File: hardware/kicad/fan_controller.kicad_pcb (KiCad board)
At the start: 2 copper layers, 75 x 60 mm, 75 parts, among them J1 12V IN, J10 AIN2, J11 AIN3, J12 AIN4, J13 AIN5, J14 AIN6, J2 BluePill A, J3 BluePill B, J5 FAN1, J6 FAN2, J7 FAN3, J8 FAN4, J9 AIN1, Q1 BSS138, Q2 BSS138, Q3 BSS138, Q4 BSS138

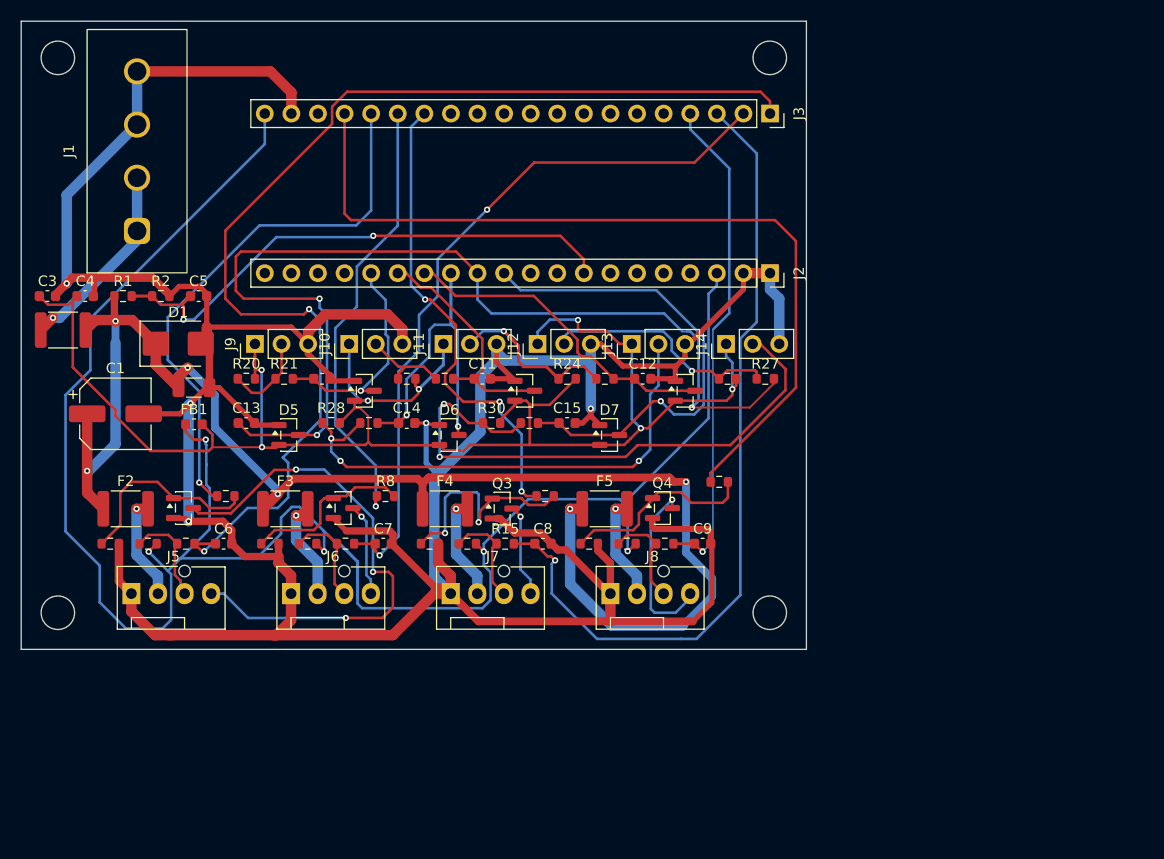
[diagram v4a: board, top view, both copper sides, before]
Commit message: DC mode support
Signed-off-by: Roman Skakun <rm.skakun@gmail.com>
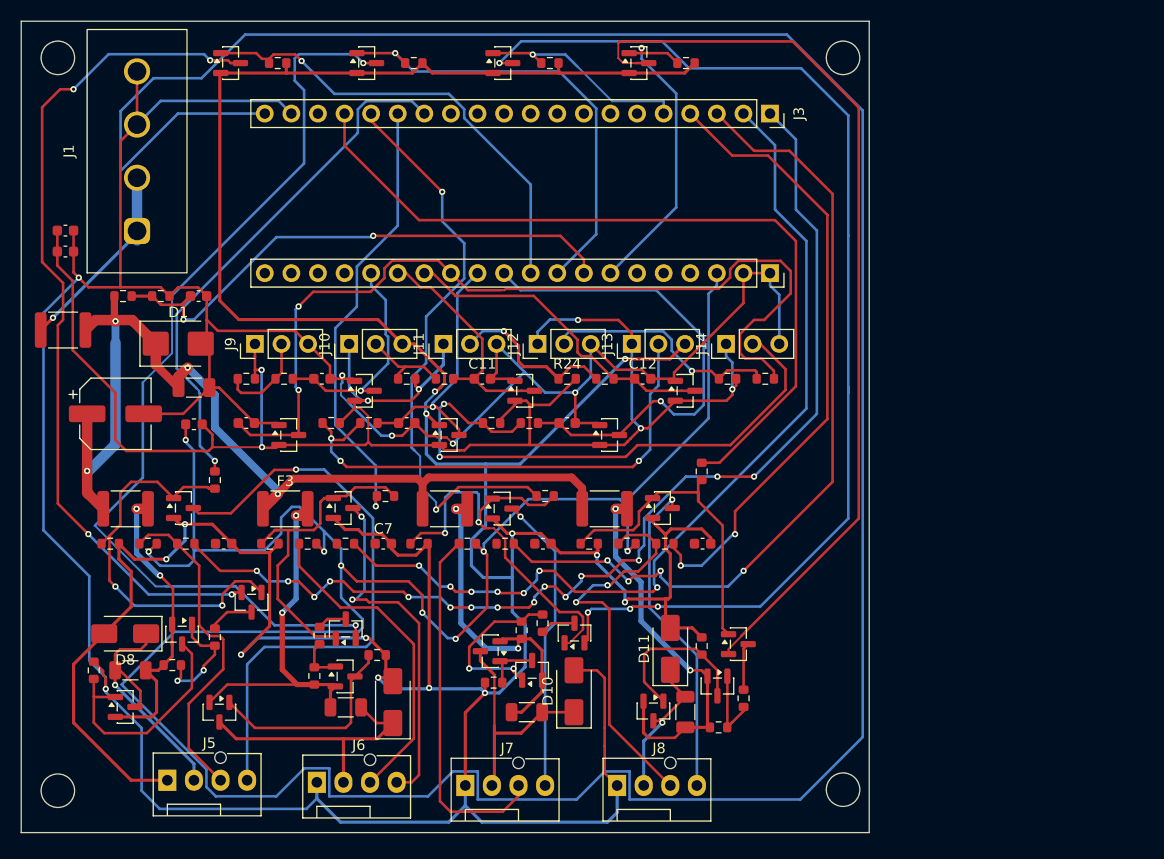
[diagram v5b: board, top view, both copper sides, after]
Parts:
- added D10: SS34, Diode_SMD:D_SMA, F.Cu at (52.8, 64.0)
- added D11: SS34, Diode_SMD:D_SMA, F.Cu at (62.0, 60.0)
- added D8: SS34, Diode_SMD:D_SMA, F.Cu at (9.93, 58.5)
- added D9: SS34, Diode_SMD:D_SMA, F.Cu at (35.5, 65.0)
- added JP1: 0, Resistor_SMD:R_1206_3216Metric, F.Cu at (10.4, 62.0)
- added JP2: 0, Resistor_SMD:R_1206_3216Metric, F.Cu at (31.0, 65.5)
- added JP3: 0, Resistor_SMD:R_1206_3216Metric, F.Cu at (48.3, 66.0)
- added JP4: 0, Resistor_SMD:R_1206_3216Metric, F.Cu at (63.4, 66.0)
- added Q10: BSS138, Package_TO_SOT_SMD:SOT-23, F.Cu at (31.0, 58.0)
- added Q11: AO3401A, Package_TO_SOT_SMD:SOT-23, F.Cu at (44.8, 60.2)
- added Q12: MMBT3906, Package_TO_SOT_SMD:SOT-23, F.Cu at (48.8, 62.0)
- added Q13: BSS138, Package_TO_SOT_SMD:SOT-23, F.Cu at (52.9, 58.4)
- added Q14: AO3401A, Package_TO_SOT_SMD:SOT-23, F.Cu at (60.4, 65.9)
- added Q15: MMBT3906, Package_TO_SOT_SMD:SOT-23, F.Cu at (66.5, 63.5)
- added Q16: BSS138, Package_TO_SOT_SMD:SOT-23, F.Cu at (68.5, 59.5)
- added Q17: BSS138, Package_TO_SOT_SMD:SOT-23, F.Cu at (20.0, 4.00)
- added Q18: BSS138, Package_TO_SOT_SMD:SOT-23, F.Cu at (33.0, 4.00)
- added Q19: BSS138, Package_TO_SOT_SMD:SOT-23, F.Cu at (46.0, 4.00)
- added Q20: BSS138, Package_TO_SOT_SMD:SOT-23, F.Cu at (59.0, 4.00)
- added Q5: AO3401A, Package_TO_SOT_SMD:SOT-23, F.Cu at (9.93, 65.5)
- added Q6: MMBT3906, Package_TO_SOT_SMD:SOT-23, F.Cu at (15.4, 58.5)
- added Q7: BSS138, Package_TO_SOT_SMD:SOT-23, F.Cu at (22.0, 55.5)
- added Q8: AO3401A, Package_TO_SOT_SMD:SOT-23, F.Cu at (18.9, 66.0)
- added Q9: MMBT3906, Package_TO_SOT_SMD:SOT-23, F.Cu at (30.9, 62.6)
- added R32: 2.2k, Resistor_SMD:R_0603_1608Metric, F.Cu at (6.93, 62.0)
- added R33: 10k, Resistor_SMD:R_0603_1608Metric, F.Cu at (14.4, 61.5)
- added R34: 4.7k, Resistor_SMD:R_0603_1608Metric, F.Cu at (18.5, 58.8)
- added R35: 2.2k, Resistor_SMD:R_0603_1608Metric, F.Cu at (34.0, 60.5)
- added R36: 10k, Resistor_SMD:R_0603_1608Metric, F.Cu at (28.0, 62.5)
- added R37: 4.7k, Resistor_SMD:R_0603_1608Metric, F.Cu at (28.5, 58.7)
- added R38: 2.2k, Resistor_SMD:R_0603_1608Metric, F.Cu at (45.1, 63.2)
- added R39: 10k, Resistor_SMD:R_0603_1608Metric, F.Cu at (47.8, 58.2)
- added R40: 4.7k, Resistor_SMD:R_0603_1608Metric, F.Cu at (49.8, 57.5)
- added R41: 2.2k, Resistor_SMD:R_0603_1608Metric, F.Cu at (65.0, 59.7)
- added R42: 10k, Resistor_SMD:R_0603_1608Metric, F.Cu at (66.6, 67.5)
- added R43: 4.7k, Resistor_SMD:R_0603_1608Metric, F.Cu at (69.0, 64.7)
- added R44: 10k, Resistor_SMD:R_0603_1608Metric, F.Cu at (24.5, 4.00)
- added R45: 10k, Resistor_SMD:R_0603_1608Metric, F.Cu at (37.5, 4.00)
- added R46: 10k, Resistor_SMD:R_0603_1608Metric, F.Cu at (50.5, 4.00)
- added R47: 10k, Resistor_SMD:R_0603_1608Metric, F.Cu at (63.5, 4.00)
- moved J7 18.4 mm to (42.4, 73.0)
- moved J8 18.3 mm to (56.9, 73.0)
- moved J6 18.2 mm to (28.2, 72.7)
- moved J5 18.2 mm to (14.0, 72.5)
- moved C3 6.49 mm to (4.22, 20.0)
- moved C4 4.66 mm to (4.22, 22.0)
- moved R16 1.95 mm to (65.0, 43.0), turned to -90 degrees
- moved R4 1.85 mm to (18.5, 43.8), turned to -90 degrees
- moved R13 1.01 mm to (38.0, 49.9)
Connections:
- net FAN1_TACH_IN renamed Net-(J5-Pad3)
- net FAN2_PWM renamed Net-(J3-Pad15)
- net FAN4_PWM renamed Net-(J3-Pad17)
- net FAN4_TACH_IN renamed Net-(J8-Pad3)
- F2 pad 2: FAN1_12V -> +12V_F1
- F3 pad 2: FAN2_12V -> Net-(F3-Pad2)
- F4 pad 2: FAN3_12V -> +12V_F3
- F5 pad 2: FAN4_12V -> +12V_F4
- J2 pad 10: (no net) -> FAN1_DCEN
- J2 pad 12: AIN4 -> AIN5
- J2 pad 13: AIN5 -> AIN4
- J2 pad 17: (no net) -> unconnected-(J2-PC15-Pad17)
- J2 pad 18: (no net) -> unconnected-(J2-PC14-Pad18)
- J2 pad 19: (no net) -> unconnected-(J2-PC13-Pad19)
- J2 pad 20: (no net) -> unconnected-(J2-VBAT-Pad20)
- J2 pad 5: (no net) -> /FAN4_SW
- J2 pad 6: (no net) -> /FAN3_SW
- J2 pad 7: (no net) -> FAN4_DCEN
- J2 pad 9: (no net) -> FAN2_DCEN
- J3 pad 1: FAN1_TACH -> Net-(J3-Pad1)
- J3 pad 10: (no net) -> /FAN1_SW
- J3 pad 11: (no net) -> /FAN2_SW
- J3 pad 12: (no net) -> unconnected-(J3-PB4-Pad12)
- J3 pad 13: (no net) -> unconnected-(J3-PB5-Pad13)
- J3 pad 14: FAN3_PWM -> Net-(J3-Pad14)
- J3 pad 16: FAN1_PWM -> Net-(J3-Pad16)
- J3 pad 2: FAN2_TACH -> Net-(J3-Pad2)
- J3 pad 3: FAN3_TACH -> Net-(J3-Pad3)
- J3 pad 4: FAN4_TACH -> Net-(J3-Pad4)
- J3 pad 5: (no net) -> FAN3_DCEN
- J3 pad 6: (no net) -> unconnected-(J3-PA9-Pad6)
- J3 pad 7: (no net) -> unconnected-(J3-PA10-Pad7)
- J6 pad 3: FAN2_TACH_IN -> Net-(J6-Pad3)
- J7 pad 3: FAN3_TACH_IN -> Net-(J7-Pad3)
- R10 pad 1: FAN2_TACH_IN -> Net-(J6-Pad3)
- R11 pad 2: FAN2_TACH -> Net-(J3-Pad2)
- R12 pad 1: FAN3_PWM -> Net-(J3-Pad16)
- R14 pad 1: FAN3_TACH_IN -> Net-(J7-Pad3)
- R15 pad 2: FAN3_TACH -> Net-(J3-Pad3)
- R19 pad 2: FAN4_TACH -> Net-(J3-Pad4)
- R4 pad 1: FAN1_PWM -> Net-(J3-Pad14)
- R7 pad 2: FAN1_TACH -> Net-(J3-Pad1)
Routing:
- net GND: track 364.3 -> 647.1 mm, vias 5 -> 19
- net +3V3: track 186.7 -> 396.7 mm, vias 5 -> 8
- net Net-(Q13-Pad2): track 0.00 -> 109.2 mm, vias 0 -> 4
- net FAN1_TACH: track 108.9 -> 0.00 mm, vias 2 -> 0
- net Net-(J3-Pad1): track 0.00 -> 105.0 mm, vias 0 -> 15
- net Net-(Q10-Pad2): track 0.00 -> 91.7 mm, vias 0 -> 2
- net Net-(Q16-Pad2): track 0.00 -> 87.7 mm
- net Net-(J3-Pad2): track 0.00 -> 87.1 mm, vias 0 -> 7
- net Net-(Q17-Pad3): track 0.00 -> 81.5 mm, vias 0 -> 4
- net Net-(J3-Pad3): track 0.00 -> 79.3 mm, vias 0 -> 4
- net FAN3_TACH: track 77.8 -> 0.00 mm, vias 1 -> 0
- net FAN2_TACH: track 68.9 -> 0.00 mm, vias 2 -> 0
- net Net-(J3-Pad4): track 0.00 -> 60.1 mm, vias 0 -> 2
- net Net-(J3-Pad16): track 0.00 -> 55.4 mm, vias 0 -> 2
- net FAN1_PWM: track 52.2 -> 0.00 mm, vias 1 -> 0
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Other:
- board size 75 x 60 mm -> 81 x 77.5 mm

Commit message: hw: fix schematic connectivity errors and sync PCB to new nets
Convert local labels to global labels so net names stop getting a
sheet-path prefix (/+12V vs +12V) on PCB sync. Add missing junction
markers at four T-tapped gate-drive/tach points that touch a crossing
wire's body but weren't bonded to it, and missing GND symbols on the
channel-1 gate-bias resistor, channel-3 flyback diode, and the AIN
clamp/filter network. Resolve a duplicate #PWR101 annotation. Sync the
PCB from the schematic now that nets match cleanly (ERC 57->17
violations, 41->13 errors).

Signed-off-by: Roman Skakun <rm.skakun@gmail.com>
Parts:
- added Q17: BSS138, Package_TO_SOT_SMD:SOT-23, F.Cu at (101.0, 30.2)
- added Q18: BSS138, Package_TO_SOT_SMD:SOT-23, F.Cu at (101.0, 34.7)
- added Q19: BSS138, Package_TO_SOT_SMD:SOT-23, F.Cu at (101.0, 39.1)
- added Q20: BSS138, Package_TO_SOT_SMD:SOT-23, F.Cu at (101.0, 43.6)
- added R44: 10k, Resistor_SMD:R_0603_1608Metric, F.Cu at (105.4, 29.3)
- added R45: 10k, Resistor_SMD:R_0603_1608Metric, F.Cu at (105.4, 31.8)
- added R46: 10k, Resistor_SMD:R_0603_1608Metric, F.Cu at (105.4, 34.3)
- added R47: 10k, Resistor_SMD:R_0603_1608Metric, F.Cu at (105.4, 36.8)
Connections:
- net Net-(F3-Pad2) renamed +12V_F2
- net Net-(J3-Pad14) renamed FAN1_PWM
- net Net-(J3-Pad15) renamed FAN2_PWM
- net Net-(J3-Pad16) renamed FAN3_PWM
- net Net-(J3-Pad17) renamed FAN4_PWM
- net Net-(J5-Pad3) renamed FAN1_TACH_IN
- net Net-(J8-Pad3) renamed FAN4_TACH_IN
- C1 pad 2: GND -> unconnected-(C1---Pad2)
- C2 pad 2: GND -> unconnected-(C2-Pad2)
- C3 pad 2: GND -> unconnected-(C3-Pad2)
- C4 pad 2: GND -> unconnected-(C4-Pad2)
- C5 pad 2: GND -> unconnected-(C5-Pad2)
- D1 pad 2: GND -> unconnected-(D1-A-Pad2)
- J1 pad 3: GND -> unconnected-(J1-Pad3)
- J1 pad 4: GND -> unconnected-(J1-Pad4)
- J2 pad 1: GND -> unconnected-(J2-GND-Pad1)
- J2 pad 2: GND -> unconnected-(J2-GND-Pad2)
- J2 pad 5: /FAN4_SW -> unconnected-(J2-PB11-Pad5)
- J2 pad 6: /FAN3_SW -> unconnected-(J2-PB10-Pad6)
- J3 pad 1: Net-(J3-Pad1) -> FAN1_TACH
- J3 pad 10: /FAN1_SW -> unconnected-(J3-PA15-Pad10)
- J3 pad 11: /FAN2_SW -> unconnected-(J3-PB3-Pad11)
- J3 pad 19: GND -> unconnected-(J3-GND-Pad19)
- J3 pad 2: Net-(J3-Pad2) -> FAN2_TACH
- J3 pad 3: Net-(J3-Pad3) -> FAN3_TACH
- J3 pad 4: Net-(J3-Pad4) -> FAN4_TACH
- J6 pad 3: Net-(J6-Pad3) -> FAN2_TACH_IN
- J7 pad 3: Net-(J7-Pad3) -> FAN3_TACH_IN
- Q10 pad 2: Net-(Q10-Pad2) -> Net-(Q10-S)
- Q13 pad 2: Net-(Q13-Pad2) -> Net-(Q13-S)
- Q16 pad 2: Net-(Q16-Pad2) -> Net-(Q16-S)
- Q7 pad 2: Net-(Q17-Pad3) -> Net-(Q17-D)
- R10 pad 1: Net-(J6-Pad3) -> FAN2_TACH_IN
- R11 pad 2: Net-(J3-Pad2) -> FAN2_TACH
- R14 pad 1: Net-(J7-Pad3) -> FAN3_TACH_IN
- R15 pad 2: Net-(J3-Pad3) -> FAN3_TACH
- R19 pad 2: Net-(J3-Pad4) -> FAN4_TACH
- R2 pad 2: GND -> unconnected-(R2-Pad2)
- R7 pad 2: Net-(J3-Pad1) -> FAN1_TACH
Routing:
- net Net-(J3-Pad1): track 105.0 -> 0.00 mm, vias 15 -> 0
- net FAN1_TACH: track 0.00 -> 105.0 mm, vias 0 -> 15
- net Net-(J3-Pad2): track 87.1 -> 0.00 mm, vias 7 -> 0
- net FAN2_TACH: track 0.00 -> 87.1 mm, vias 0 -> 7
- net Net-(J3-Pad3): track 79.3 -> 0.00 mm, vias 4 -> 0
- net FAN3_TACH: track 0.00 -> 79.3 mm, vias 0 -> 4
- net Net-(J3-Pad4): track 60.1 -> 0.00 mm, vias 2 -> 0
- net FAN4_TACH: track 0.00 -> 60.1 mm, vias 0 -> 2
- net Net-(J7-Pad3): track 34.9 -> 0.00 mm
- net FAN3_TACH_IN: track 0.00 -> 34.9 mm
- net Net-(J6-Pad3): track 31.1 -> 0.00 mm
- net FAN2_TACH_IN: track 0.00 -> 31.1 mm

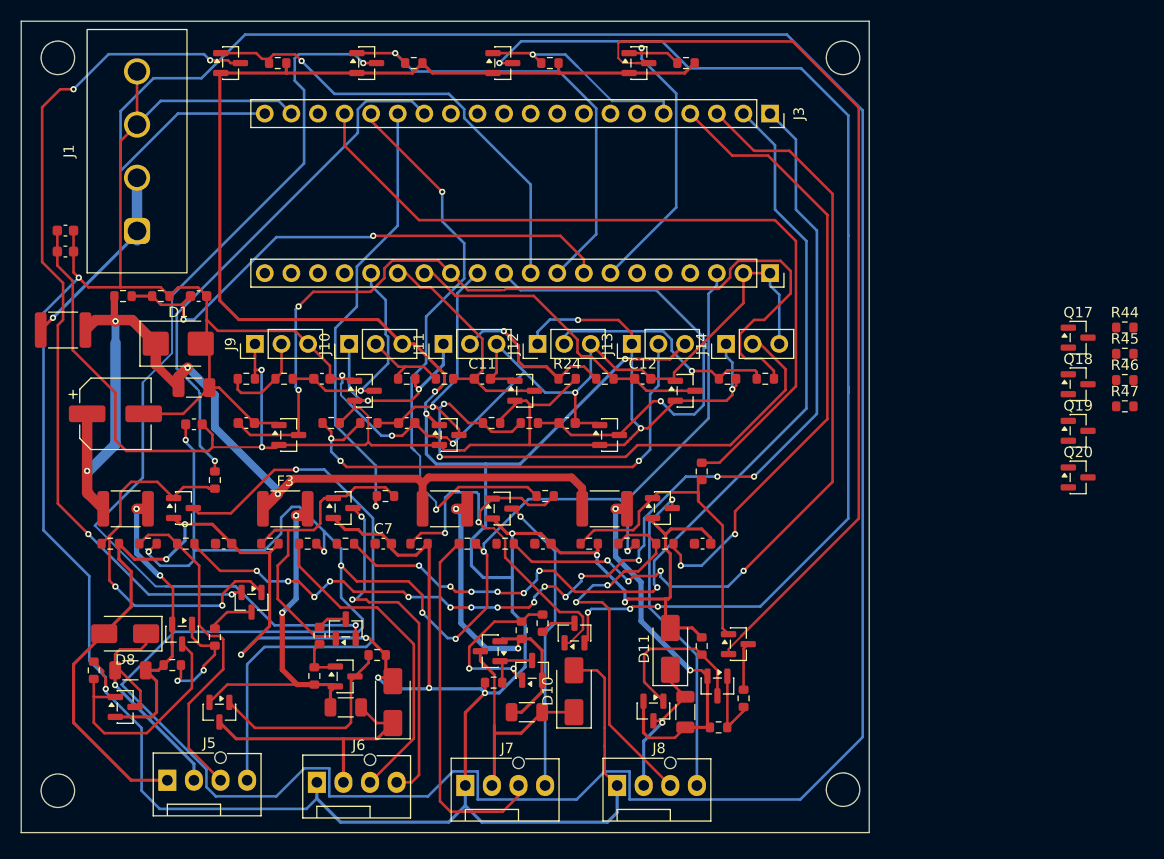
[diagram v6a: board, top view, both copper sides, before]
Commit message: hw: clean up motor-switch duplicate footprints and dead-net shorts
Remove stray duplicate Q17/Q18/Q19/Q20 (Q_en) and R44-R47 (R_dcen)
footprints left over from PCB sync, and delete the leftover copper on
the resulting dead Net-(Qn-...) nets that was shorting the live
Q_inv/Q_en cascode nets (Net-(Q13-S), Net-(Q16-S), Net-(Q17-D)).
Reconnect J2 pin1/pin2 to GND in the schematic (found floating, no
wire or power symbol). Align the 4 board-perimeter bolt holes into a
clean rectangle (one corner was 0.1mm off). DRC shorting_items for
this feature's nets cleared; remaining DRC errors are pre-existing and
out of scope.

Signed-off-by: Roman Skakun <rm.skakun@gmail.com>
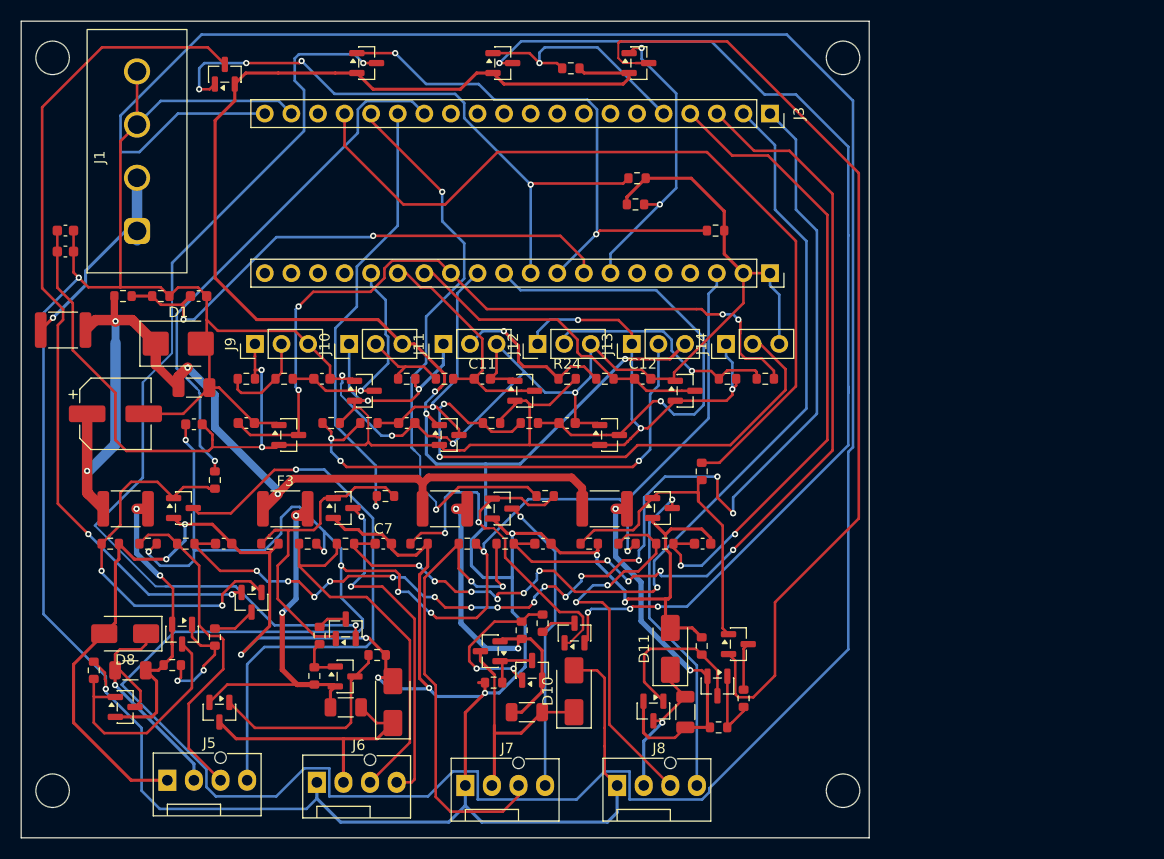
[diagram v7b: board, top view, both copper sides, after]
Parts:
- removed the Q17 at (101.0, 30.2)
- removed the Q17 at (20.0, 4.00)
- removed the Q18 at (101.0, 34.7)
- removed the Q19 at (101.0, 39.1)
- removed the Q20 at (101.0, 43.6)
- removed the R44 at (24.5, 4.00)
- removed the R45 at (37.5, 4.00)
- removed the R46 at (50.5, 4.00)
- removed the R47 at (63.5, 4.00)
- added Q17: BSS138, Package_TO_SOT_SMD:SOT-23, F.Cu at (19.4, 5.06)
- moved R46 60.7 mm to (52.5, 4.50)
- moved R47 50.6 mm to (58.7, 17.5), turned to 180 degrees
- moved R44 48.7 mm to (58.8, 15.0)
- moved R45 40.8 mm to (66.3, 20.0)
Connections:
- C1 pad 2: unconnected-(C1---Pad2) -> GND
- C2 pad 2: unconnected-(C2-Pad2) -> GND
- C3 pad 2: unconnected-(C3-Pad2) -> GND
- C4 pad 2: unconnected-(C4-Pad2) -> GND
- C5 pad 2: unconnected-(C5-Pad2) -> GND
- D1 pad 2: unconnected-(D1-A-Pad2) -> GND
- J1 pad 3: unconnected-(J1-Pad3) -> GND
- J1 pad 4: unconnected-(J1-Pad4) -> GND
- J2 pad 1: unconnected-(J2-GND-Pad1) -> GND
- J2 pad 2: unconnected-(J2-GND-Pad2) -> GND
- J3 pad 19: unconnected-(J3-GND-Pad19) -> GND
- Q13 pad 2: Net-(Q13-S) -> Net-(Q13-Pad2)
- Q16 pad 2: Net-(Q16-S) -> Net-(Q16-Pad2)
- Q18 pad 3: Net-(Q10-Pad2) -> Net-(Q10-S)
- R2 pad 2: unconnected-(R2-Pad2) -> GND
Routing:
- net Net-(Q10-S): track 0.00 -> 91.7 mm, vias 0 -> 2
- net Net-(Q10-Pad2): track 91.7 -> 0.00 mm, vias 2 -> 0
- net Net-(Q17-Pad3): track 81.5 -> 0.00 mm, vias 4 -> 0
- net Net-(Q17-D): track 0.00 -> 80.6 mm, vias 0 -> 2
- net GND: track 647.1 -> 662.2 mm
- net FAN1_DCEN: track 44.5 -> 59.4 mm, vias 1 -> 4
- net AIN4: track 86.4 -> 73.4 mm, vias 2 -> 4
- net FAN3_TACH_IN: track 34.9 -> 47.7 mm, vias 0 -> 2
- net +3V3: track 396.7 -> 386.1 mm
- net FAN2_DCEN: track 43.7 -> 53.1 mm, vias 1 -> 2
- net FAN1_TACH: track 105.0 -> 113.5 mm
- net Net-(Q13-Pad2): track 109.2 -> 103.5 mm
- net Net-(Q16-Pad2): track 87.7 -> 93.1 mm
- net FAN3_DCEN: track 20.5 -> 25.5 mm
- net FAN2_TACH_IN: track 31.1 -> 35.9 mm
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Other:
- board size 81 x 77.5 mm -> 81 x 78 mm
